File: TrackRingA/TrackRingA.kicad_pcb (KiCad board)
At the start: 2 copper layers, 15 x 15 mm, 14 parts, among them J1 Conn_01x04, U1 TLV493D-A1B6, U2 LIS2DTW12

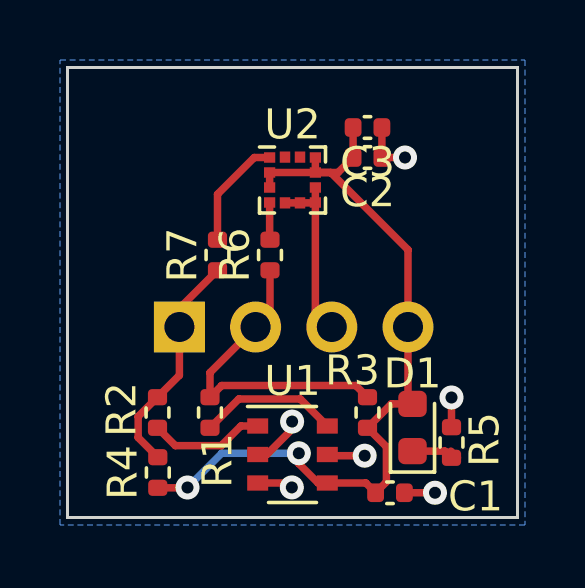
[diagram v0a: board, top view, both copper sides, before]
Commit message: Finished BusChain1.1 and added power daisy-chaining option
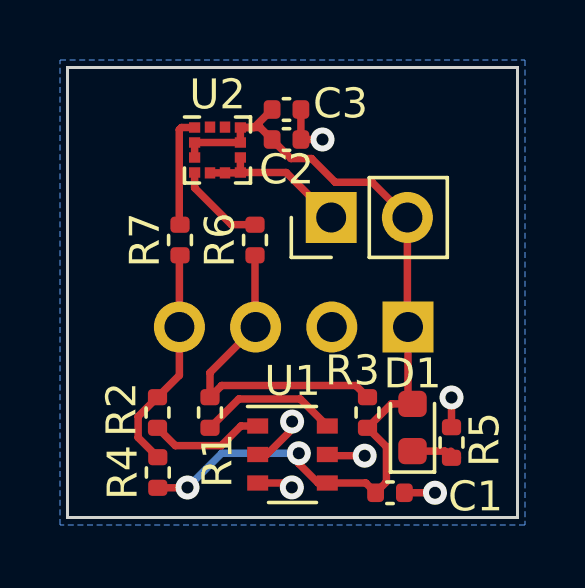
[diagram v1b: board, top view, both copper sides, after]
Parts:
- added J2: Conn_01x02, Connector_PinHeader_2.54mm:PinHeader_1x02_P2.54mm_Vertical, F.Cu at (27.3, 25.0)
- J1: footprint Connector_PinSocket_2.54mm:PinSocket_1x04_P2.54mm_Horizontal -> Connector_PinHeader_2.54mm:PinHeader_1x04_P2.54mm_Vertical
- moved J1 7.62 mm to (29.9, 28.6), turned to 90 degrees
- moved C2 2.77 mm to (25.8, 22.4)
- moved C3 2.77 mm to (25.8, 21.4)
- moved U2 2.69 mm to (23.5, 22.8)
- moved R7 1.35 mm to (22.2, 25.8)
- moved R6 0.71 mm to (24.8, 25.8)
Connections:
- J1 pad 1: /SCL -> /VCC
- J1 pad 2: /SDA -> GND
- J1 pad 3: GND -> /SDA
- J1 pad 4: /VCC -> /SCL
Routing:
- net /VCC: track 27.2 -> 29.8 mm
- net Net-(U2-SDA/SDI/SDO): track 1.25 -> 3.03 mm
- net GND: track 13.9 -> 13.1 mm
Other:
- board text added: "TrackNode 1.1"
- board text removed: "TrackRing 1.0"
